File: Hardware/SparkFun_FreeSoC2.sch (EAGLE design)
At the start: 107 parts, among them U1 CY8C5888AXI-LP096, U2 MIC5219 5V, U3 MIC5219 3.3V, U4 2A/20V, U7 CY8C5868LTI-LP039, Y1 32.768kHz

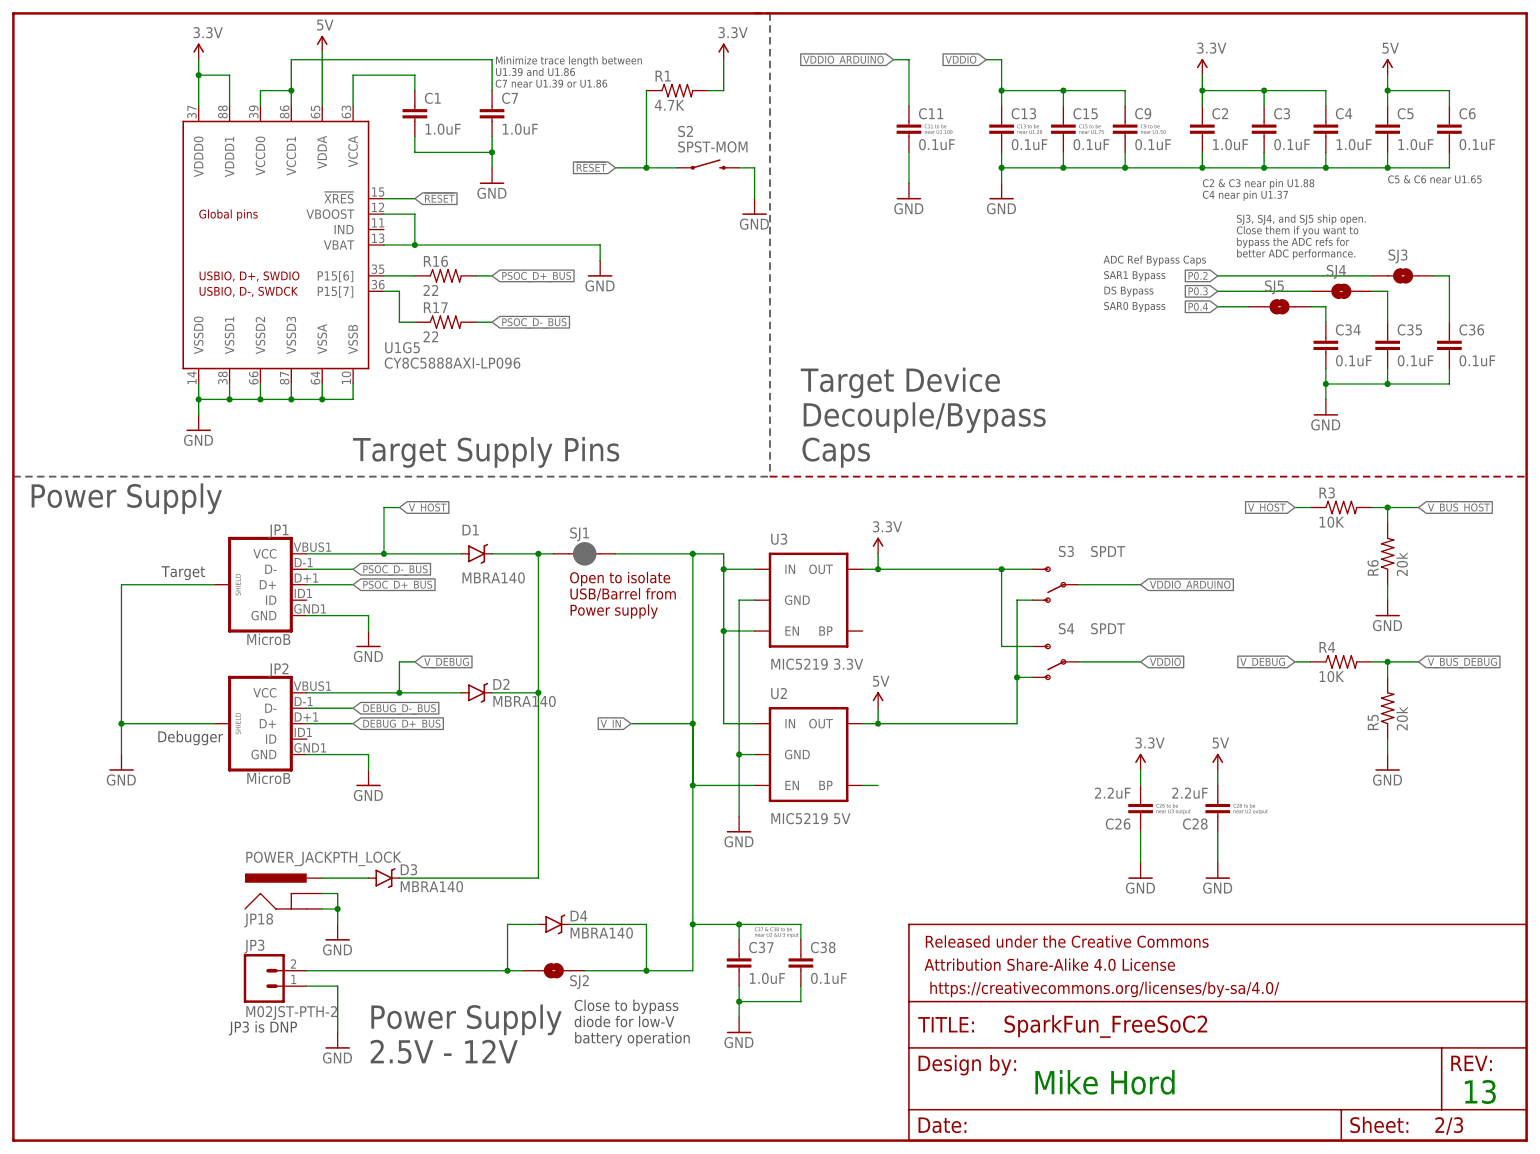
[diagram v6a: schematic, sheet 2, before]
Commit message: Add small series resistor on regulator bypass caps
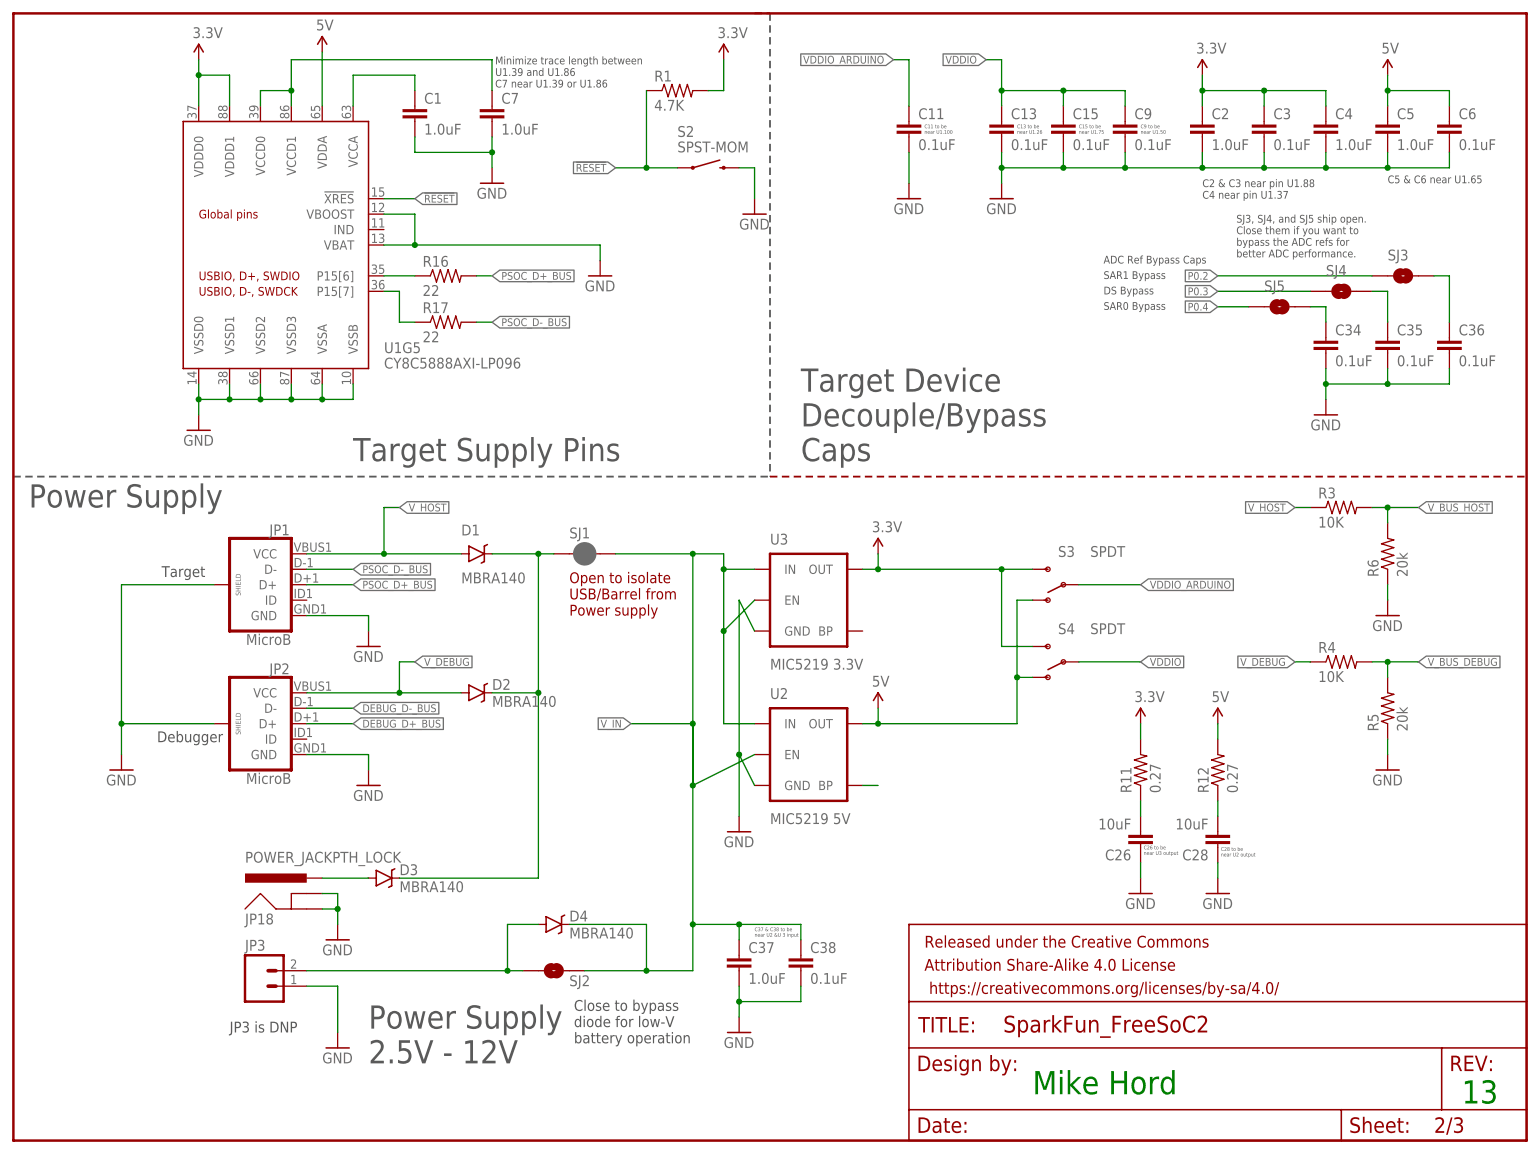
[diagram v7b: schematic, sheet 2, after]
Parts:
- added R11, R12: 0.27, SparkFun-Resistors:0.27OHM-1/10W-1%(0603)
- C26, C28: value 2.2uF -> 10uF; device SparkFun-Capacitors:2.2UF-10V-20%(0603) -> SparkFun-Capacitors:10UF10V10%(0805)
- JP3: value M02JST-PTH-2 -> (none)
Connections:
- new net N$1: C26.2, R11.1
- new net N$6: C28.2, R12.1
- net 3.3V: now also R11.2; no longer C26.2
- net 5V: now also R12.2; no longer C28.2
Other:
- moved on the sheet: C26, C28
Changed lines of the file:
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@@
 <layer number="113" name="IDFDebug" color="7" fill="1" visible="yes" active="yes"/>
 <layer number="116" name="Patch_BOT" color="9" fill="4" visible="no" active="yes"/>
+<layer number="118" name="Rect_Pads" color="7" fill="1" visible="yes" active="yes"/>
 <layer number="121" name="_tsilk" color="7" fill="1" visible="no" active="yes"/>
 <layer number="122" name="_bsilk" color="7" fill="1" visible="no" active="yes"/>
@@
 <part name="GND10" library="SparkFun-Aesthetics" deviceset="GND" device=""/>
 <part name="GND11" library="SparkFun-Aesthetics" deviceset="GND" device=""/>
-<part name="C26" library="SparkFun-Capacitors" deviceset="2.2UF-10V-20%(0603)" device="" value="2.2uF"/>
-<part name="C28" library="SparkFun-Capacitors" deviceset="2.2UF-10V-20%(0603)" device="" value="2.2uF"/>
+<part name="C26" library="SparkFun-Capacitors" deviceset="10UF10V10%(0805)" device="" value="10uF"/>
+<part name="C28" library="SparkFun-Capacitors" deviceset="10UF10V10%(0805)" device="" value="10uF"/>
 <part name="SUPPLY9" library="SparkFun-Aesthetics" deviceset="5V" device=""/>
 <part name="SUPPLY10" library="SparkFun-Aesthetics" deviceset="3.3V" device=""/>
@@
 <part name="C38" library="SparkFun-Capacitors" deviceset="0.1UF-25V(+80/-20%)(0603)" device="" value="0.1uF"/>
 <part name="GND40" library="SparkFun-Aesthetics" deviceset="GND" device=""/>
+<part name="R11" library="SparkFun-Resistors" deviceset="0.27OHM-1/10W-1%(0603)" device="" value="0.27"/>
+<part name="R12" library="SparkFun-Resistors" deviceset="0.27OHM-1/10W-1%(0603)" device="" value="0.27"/>
 </parts>
 <sheets>
@@
 <text x="175.26" y="165.608" size="0.6096" layer="97">C15 to be
 near U1.75</text>
-<text x="187.96" y="53.848" size="0.6096" layer="97">C26 to be
+<text x="185.928" y="46.99" size="0.6096" layer="97">C26 to be
 near U3 output</text>
-<text x="200.66" y="53.848" size="0.6096" layer="97">C28 to be
+<text x="198.628" y="46.736" size="0.6096" layer="97">C28 to be
 near U2 output</text>
 <text x="179.324" y="141.732" size="1.27" layer="97">SAR1 Bypass</text>
@@
 <instance part="SUPPLY3" gate="G$1" x="50.8" y="179.07"/>
 <instance part="GND5" gate="1" x="17.78" y="60.96"/>
-<instance part="C26" gate="G$1" x="185.42" y="55.88" rot="R180"/>
-<instance part="C28" gate="G$1" x="198.12" y="55.88" rot="R180"/>
-<instance part="SUPPLY9" gate="G$1" x="198.12" y="60.96"/>
-<instance part="SUPPLY10" gate="G$1" x="185.42" y="60.96"/>
-<instance part="GND13" gate="1" x="198.12" y="43.18"/>
+<instance part="C26" gate="G$1" x="185.42" y="50.8" rot="R180"/>
+<instance part="C28" gate="G$1" x="198.12" y="50.8" rot="R180"/>
+<instance part="SUPPLY9" gate="G$1" x="198.12" y="68.58"/>
+<instance part="SUPPLY10" gate="G$1" x="185.42" y="68.58"/>
+<instance part="GND13" gate="1" x="198.12" y="40.64"/>
 <instance part="SUPPLY11" gate="G$1" x="226.06" y="175.26"/>
 <instance part="C34" gate="G$1" x="215.9" y="129.54"/>
@@
 <instance part="FRAME2" gate="G$1" x="0" y="0"/>
 <instance part="FRAME2" gate="V" x="147.32" y="0"/>
-<instance part="GND34" gate="1" x="185.42" y="43.18"/>
+<instance part="GND34" gate="1" x="185.42" y="40.64"/>
 <instance part="C37" gate="G$1" x="119.38" y="27.94"/>
 <instance part="C38" gate="G$1" x="129.54" y="27.94"/>
 <instance part="GND40" gate="1" x="119.38" y="17.78"/>
+<instance part="R11" gate="G$1" x="185.42" y="60.96" rot="R90"/>
+<instance part="R12" gate="G$1" x="198.12" y="60.96" rot="R90"/>
 </instances>
 <busses>
@@
 <wire x1="119.38" y1="53.34" x2="119.38" y2="63.5" width="0.1524" layer="91"/>
 <pinref part="U2" gate="G$1" pin="GND"/>
-<wire x1="119.38" y1="63.5" x2="121.92" y2="63.5" width="0.1524" layer="91"/>
+<wire x1="119.38" y1="63.5" x2="121.92" y2="58.42" width="0.1524" layer="91"/>
 <wire x1="119.38" y1="63.5" x2="119.38" y2="88.9" width="0.1524" layer="91"/>
 <junction x="119.38" y="63.5"/>
 <pinref part="U3" gate="G$1" pin="GND"/>
-<wire x1="119.38" y1="88.9" x2="121.92" y2="88.9" width="0.1524" layer="91"/>
+<wire x1="119.38" y1="88.9" x2="121.92" y2="83.82" width="0.1524" layer="91"/>
 </segment>
 <segment>
@@
 <pinref part="GND34" gate="1" pin="GND"/>
 <pinref part="C26" gate="G$1" pin="1"/>
-<wire x1="185.42" y1="50.8" x2="185.42" y2="45.72" width="0.1524" layer="91"/>
+<wire x1="185.42" y1="45.72" x2="185.42" y2="43.18" width="0.1524" layer="91"/>
 </segment>
 <segment>
 <pinref part="GND13" gate="1" pin="GND"/>
 <pinref part="C28" gate="G$1" pin="1"/>
-<wire x1="198.12" y1="45.72" x2="198.12" y2="50.8" width="0.1524" layer="91"/>
+<wire x1="198.12" y1="43.18" x2="198.12" y2="45.72" width="0.1524" layer="91"/>
 </segment>
 <segment>
@@
 <wire x1="116.84" y1="93.98" x2="121.92" y2="93.98" width="0.1524" layer="91"/>
 <pinref part="U3" gate="G$1" pin="EN"/>
-<wire x1="121.92" y1="83.82" x2="116.84" y2="83.82" width="0.1524" layer="91"/>
+<wire x1="121.92" y1="88.9" x2="116.84" y2="83.82" width="0.1524" layer="91"/>
 <junction x="116.84" y="83.82"/>
 <pinref part="U2" gate="G$1" pin="EN"/>
-<wire x1="121.92" y1="58.42" x2="111.76" y2="58.42" width="0.1524" layer="91"/>
+<wire x1="121.92" y1="63.5" x2="111.76" y2="58.42" width="0.1524" layer="91"/>
 <junction x="111.76" y="58.42"/>
 <wire x1="111.76" y1="96.52" x2="116.84" y2="96.52" width="0.1524" layer="91"/>
@@
 </segment>
 <segment>
-<pinref part="SUPPLY10" gate="G$1" pin="3.3V"/>
-<pinref part="C26" gate="G$1" pin="2"/>
-<wire x1="185.42" y1="60.96" x2="185.42" y2="58.42" width="0.1524" layer="91"/>
-</segment>
-<segment>
 <pinref part="U1" gate="G5" pin="VDDD0"/>
 <pinref part="U1" gate="G5" pin="VDDD1"/>
@@
 <wire x1="116.84" y1="177.8" x2="116.84" y2="172.72" width="0.1524" layer="91"/>
 <wire x1="116.84" y1="172.72" x2="114.3" y2="172.72" width="0.1524" layer="91"/>
+</segment>
+<segment>
+<pinref part="SUPPLY10" gate="G$1" pin="3.3V"/>
+<pinref part="R11" gate="G$1" pin="2"/>
+<wire x1="185.42" y1="68.58" x2="185.42" y2="66.04" width="0.1524" layer="91"/>
 </segment>
 </net>
@@
 </segment>
 <segment>
-<pinref part="SUPPLY9" gate="G$1" pin="5V"/>
-<pinref part="C28" gate="G$1" pin="2"/>
-<wire x1="198.12" y1="60.96" x2="198.12" y2="58.42" width="0.1524" layer="91"/>
-</segment>
-<segment>
 <pinref part="C5" gate="G$1" pin="1"/>
 <pinref part="C6" gate="G$1" pin="1"/>
@@
 <pinref part="SUPPLY3" gate="G$1" pin="5V"/>
 </segment>
+<segment>
+<pinref part="SUPPLY9" gate="G$1" pin="5V"/>
+<pinref part="R12" gate="G$1" pin="2"/>
+<wire x1="198.12" y1="68.58" x2="198.12" y2="66.04" width="0.1524" layer="91"/>
+</segment>
 </net>
 <net name="P0.2" class="0">
@@
 </segment>
 </net>
+<net name="N$1" class="0">
+<segment>
+<pinref part="C26" gate="G$1" pin="2"/>
+<pinref part="R11" gate="G$1" pin="1"/>
+<wire x1="185.42" y1="53.34" x2="185.42" y2="55.88" width="0.1524" layer="91"/>
+</segment>
+</net>
+<net name="N$6" class="0">
+<segment>
+<pinref part="C28" gate="G$1" pin="2"/>
+<pinref part="R12" gate="G$1" pin="1"/>
+<wire x1="198.12" y1="53.34" x2="198.12" y2="55.88" width="0.1524" layer="91"/>
+</segment>
+</net>

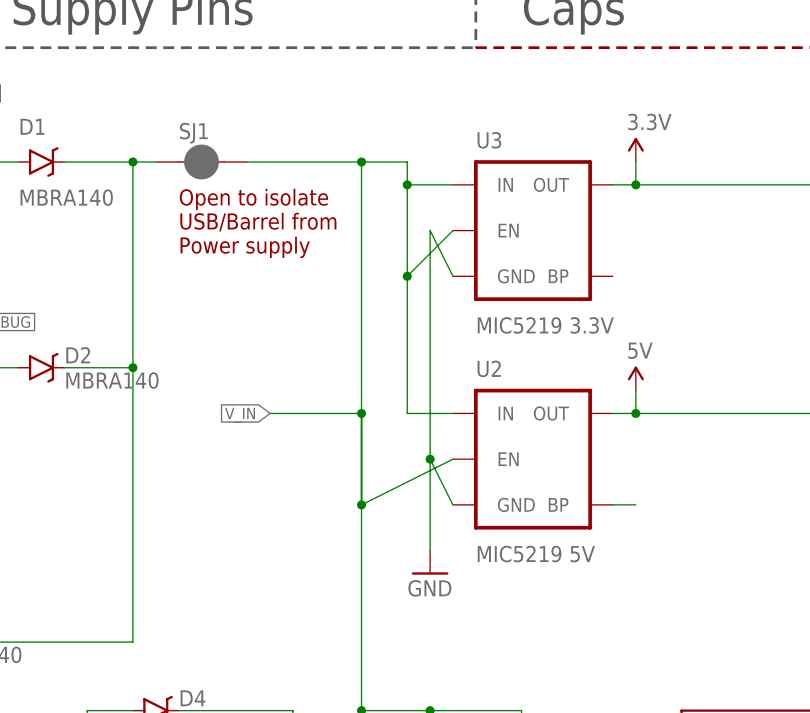
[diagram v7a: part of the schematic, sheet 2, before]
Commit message: Schematic fixes from QC feedback
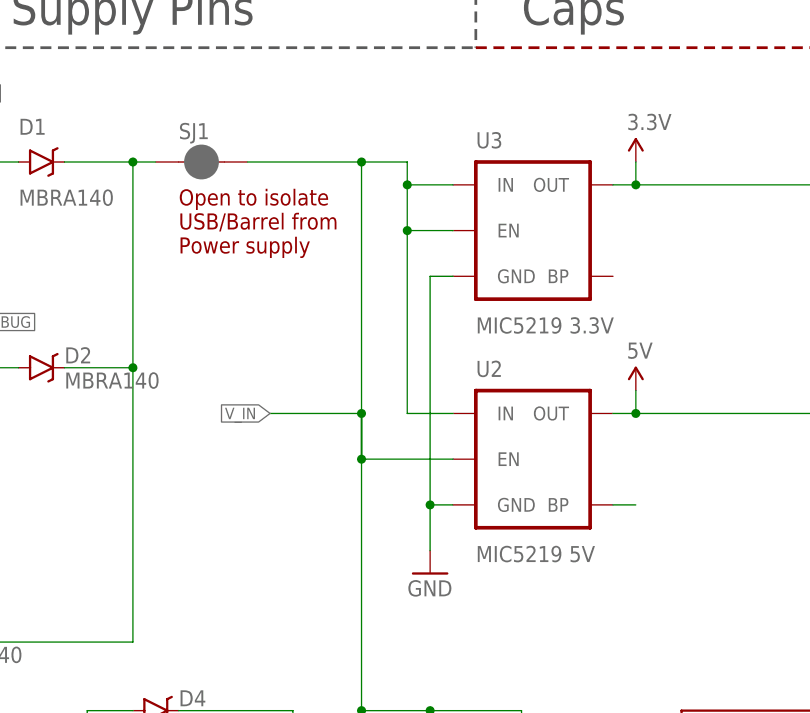
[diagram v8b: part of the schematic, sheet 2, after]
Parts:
- R11, R12: PROD_ID (none) -> RES-08787
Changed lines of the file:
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@@
 <part name="C38" library="SparkFun-Capacitors" deviceset="0.1UF-25V(+80/-20%)(0603)" device="" value="0.1uF"/>
 <part name="GND40" library="SparkFun-Aesthetics" deviceset="GND" device=""/>
-<part name="R11" library="SparkFun-Resistors" deviceset="0.27OHM-1/10W-1%(0603)" device="" value="0.27"/>
-<part name="R12" library="SparkFun-Resistors" deviceset="0.27OHM-1/10W-1%(0603)" device="" value="0.27"/>
+<part name="R11" library="SparkFun-Resistors" deviceset="0.27OHM-1/10W-1%(0603)" device="" value="0.27">
+<attribute name="PROD_ID" value="RES-08787"/>
+</part>
+<part name="R12" library="SparkFun-Resistors" deviceset="0.27OHM-1/10W-1%(0603)" device="" value="0.27">
+<attribute name="PROD_ID" value="RES-08787"/>
+</part>
 </parts>
 <sheets>
@@
 <instance part="C38" gate="G$1" x="129.54" y="27.94"/>
 <instance part="GND40" gate="1" x="119.38" y="17.78"/>
-<instance part="R11" gate="G$1" x="185.42" y="60.96" rot="R90"/>
-<instance part="R12" gate="G$1" x="198.12" y="60.96" rot="R90"/>
+<instance part="R11" gate="G$1" x="185.42" y="60.96" rot="R90">
+<attribute name="PROD_ID" x="185.42" y="60.96" size="1.778" layer="96" rot="R90" display="off"/>
+</instance>
+<instance part="R12" gate="G$1" x="198.12" y="60.96" rot="R90">
+<attribute name="PROD_ID" x="198.12" y="60.96" size="1.778" layer="96" rot="R90" display="off"/>
+</instance>
 </instances>
 <busses>
@@
 <segment>
 <pinref part="GND1" gate="1" pin="GND"/>
-<wire x1="119.38" y1="53.34" x2="119.38" y2="63.5" width="0.1524" layer="91"/>
+<wire x1="119.38" y1="53.34" x2="119.38" y2="58.42" width="0.1524" layer="91"/>
 <pinref part="U2" gate="G$1" pin="GND"/>
-<wire x1="119.38" y1="63.5" x2="121.92" y2="58.42" width="0.1524" layer="91"/>
-<wire x1="119.38" y1="63.5" x2="119.38" y2="88.9" width="0.1524" layer="91"/>
-<junction x="119.38" y="63.5"/>
+<wire x1="119.38" y1="58.42" x2="121.92" y2="58.42" width="0.1524" layer="91"/>
+<wire x1="119.38" y1="58.42" x2="119.38" y2="83.82" width="0.1524" layer="91"/>
+<junction x="119.38" y="58.42"/>
 <pinref part="U3" gate="G$1" pin="GND"/>
-<wire x1="119.38" y1="88.9" x2="121.92" y2="83.82" width="0.1524" layer="91"/>
+<wire x1="119.38" y1="83.82" x2="121.92" y2="83.82" width="0.1524" layer="91"/>
 </segment>
 <segment>
@@
 <pinref part="SJ2" gate="G$1" pin="2"/>
 <wire x1="93.98" y1="27.94" x2="104.14" y2="27.94" width="0.1524" layer="91"/>
-<wire x1="111.76" y1="68.58" x2="111.76" y2="58.42" width="0.1524" layer="91"/>
+<wire x1="111.76" y1="68.58" x2="111.76" y2="63.5" width="0.1524" layer="91"/>
 <pinref part="SJ1" gate="G$1" pin="2"/>
-<wire x1="111.76" y1="58.42" x2="111.76" y2="96.52" width="0.1524" layer="91"/>
+<wire x1="111.76" y1="63.5" x2="111.76" y2="96.52" width="0.1524" layer="91"/>
 <wire x1="99.06" y1="96.52" x2="111.76" y2="96.52" width="0.1524" layer="91"/>
 <wire x1="111.76" y1="68.58" x2="101.6" y2="68.58" width="0.1524" layer="91"/>
@@
 <wire x1="111.76" y1="35.56" x2="111.76" y2="68.58" width="0.1524" layer="91"/>
 <wire x1="116.84" y1="68.58" x2="121.92" y2="68.58" width="0.1524" layer="91"/>
-<wire x1="116.84" y1="68.58" x2="116.84" y2="83.82" width="0.1524" layer="91"/>
+<wire x1="116.84" y1="68.58" x2="116.84" y2="88.9" width="0.1524" layer="91"/>
 <pinref part="U3" gate="G$1" pin="IN"/>
-<wire x1="116.84" y1="83.82" x2="116.84" y2="93.98" width="0.1524" layer="91"/>
+<wire x1="116.84" y1="88.9" x2="116.84" y2="93.98" width="0.1524" layer="91"/>
 <wire x1="116.84" y1="93.98" x2="121.92" y2="93.98" width="0.1524" layer="91"/>
 <pinref part="U3" gate="G$1" pin="EN"/>
-<wire x1="121.92" y1="88.9" x2="116.84" y2="83.82" width="0.1524" layer="91"/>
-<junction x="116.84" y="83.82"/>
+<wire x1="121.92" y1="88.9" x2="116.84" y2="88.9" width="0.1524" layer="91"/>
+<junction x="116.84" y="88.9"/>
 <pinref part="U2" gate="G$1" pin="EN"/>
-<wire x1="121.92" y1="63.5" x2="111.76" y2="58.42" width="0.1524" layer="91"/>
-<junction x="111.76" y="58.42"/>
+<wire x1="121.92" y1="63.5" x2="111.76" y2="63.5" width="0.1524" layer="91"/>
+<junction x="111.76" y="63.5"/>
 <wire x1="111.76" y1="96.52" x2="116.84" y2="96.52" width="0.1524" layer="91"/>
 <wire x1="116.84" y1="96.52" x2="116.84" y2="93.98" width="0.1524" layer="91"/>
